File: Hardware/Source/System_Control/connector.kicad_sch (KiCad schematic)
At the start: 28 parts, among them J10 NTC_CONN, J11 NTC_CONN, J12 NTC_CONN, J13 NTC_CONN, J14 NTC_CONN, J15 NTC_CONN, J16 BAL_BAT_CONN2, J17 NTC_CONN, J18 NTC_CONN, J19 NTC_CONN, J20 NTC_CONN, J21 NTC_CONN, J22 NTC_CONN, J23 NTC_CONN, J24 NTC_CONN, J3 SIGNAL_CONN, J4 HB9500M-9.5-2P, J5 FLASH_CONN, J6 HB9500M-9.5-2P, J7 BAL_BAT_CONN1, J8 NTC_CONN, J9 NTC_CONN

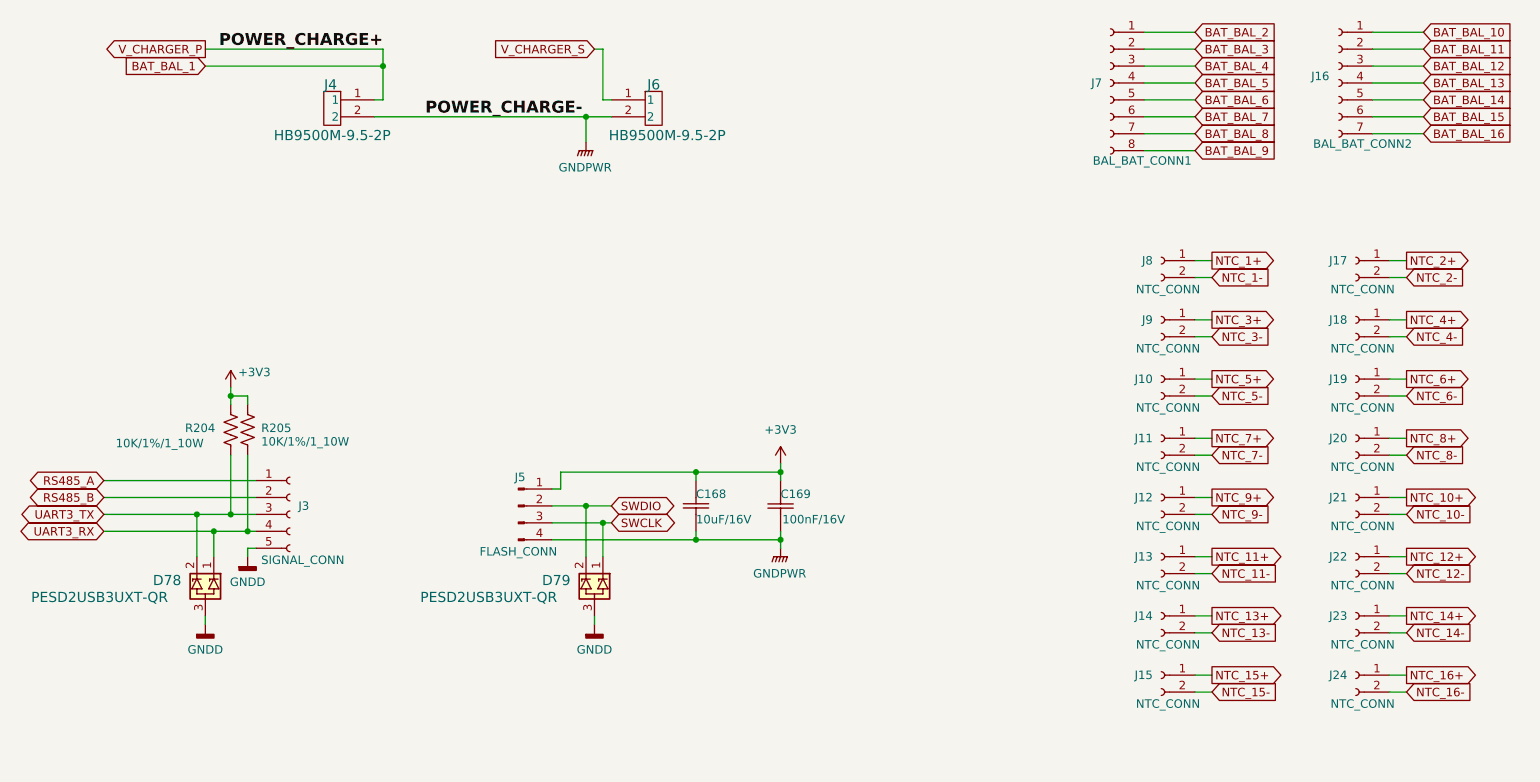
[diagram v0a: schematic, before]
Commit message: schematic: update connector charger board F4
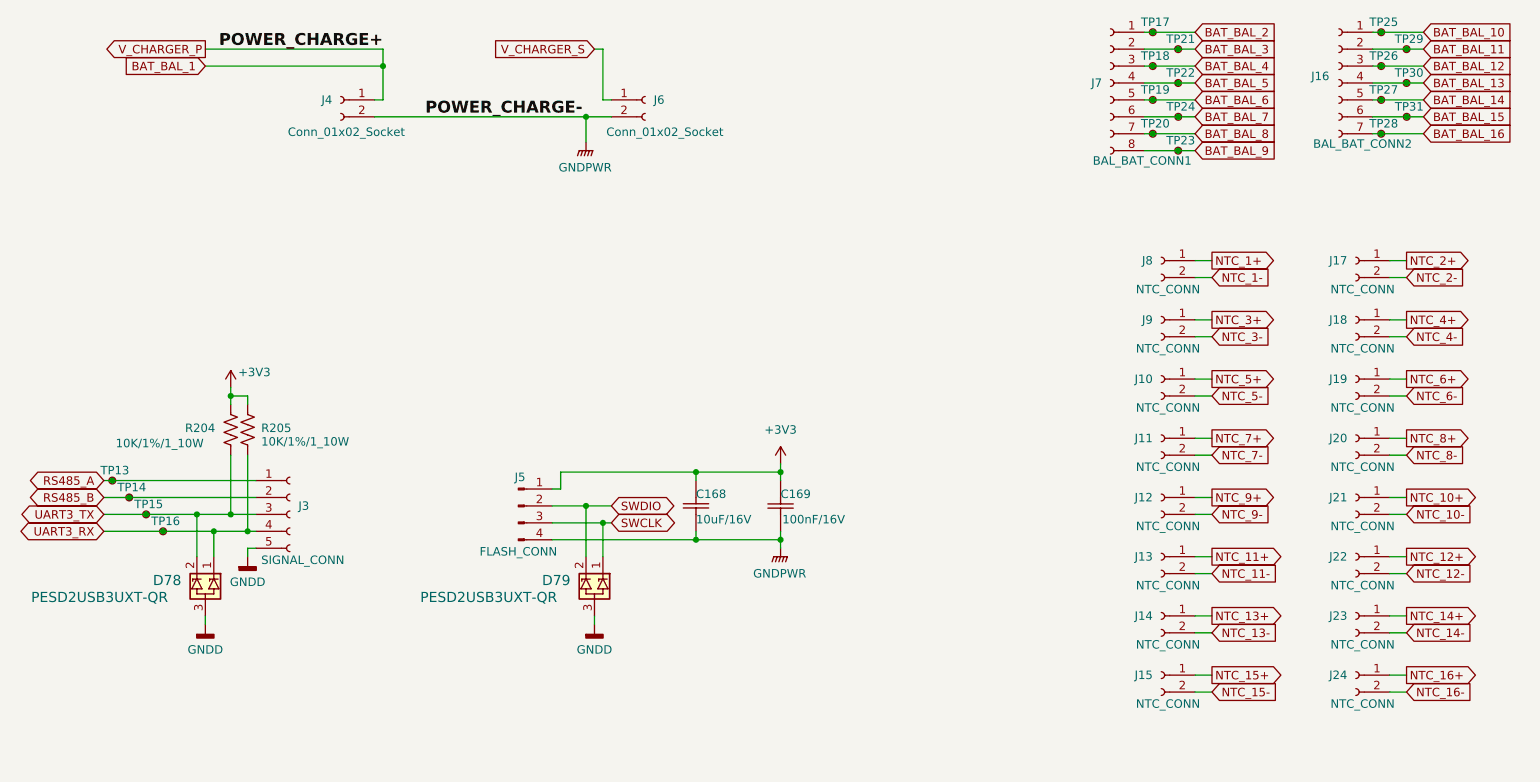
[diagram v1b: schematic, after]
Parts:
- removed J4, J6: HB9500M-9.5-2P, charge_battery_footprint_lib:CONN2_HB9500_KAN, symbol charge_battery_sym_lib:HB9500M-9.5-2P
- added J4, J6: Conn_01x02_Socket, Connector_Phoenix_MC:PhoenixContact_MC_1,5_2-G-3.81_1x02_P3.81mm_Horizontal, symbol Connector:Conn_01x02_Socket
- added TP13, TP14, TP15, TP16, TP17, TP18, TP19, TP20, TP21, TP22, TP23, TP24, TP25, TP26, TP27, TP28, TP29, TP30, TP31: TestPoint_Small, TestPoint:TestPoint_Pad_D1.0mm, symbol Connector:TestPoint_Small
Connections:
- net BAT_BAL_1: now also J4.1 (Pin_1)
- net BAT_BAL_10: now also TP25.1
- net BAT_BAL_11: now also TP29.1
- net BAT_BAL_12: now also TP26.1
- net BAT_BAL_13: now also TP30.1
- net BAT_BAL_14: now also TP27.1
- net BAT_BAL_15: now also TP31.1
- net BAT_BAL_16: now also TP28.1
- net BAT_BAL_2: now also TP17.1
- net BAT_BAL_3: now also TP21.1
- net BAT_BAL_4: now also TP18.1
- net BAT_BAL_5: now also TP22.1
- net BAT_BAL_6: now also TP19.1
- net BAT_BAL_7: now also TP24.1
- net BAT_BAL_8: now also TP20.1
- net BAT_BAL_9: now also TP23.1
- net GNDPWR: now also J4.2 (Pin_2), J6.2 (Pin_2)
- net RS485_A: now also TP13.1
- net RS485_B: now also TP14.1
- net UART3_RX: now also TP16.1
- net UART3_TX: now also TP15.1
- net V_CHARGER_S: now also J6.1 (Pin_1)

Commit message: pcb,lib,sche: PFC, lib: update pcb PFC, lib
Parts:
- renumbered C168 to C173, C169 to C174, D78 to D77, D79 to D78, R204 to R206, R205 to R207
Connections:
- net V_CHARGER_S is gone; now on net BAT_BAL_1: J6.1 (Pin_1)
- net BAT_BAL_1: no longer J4.1 (Pin_1)
- net BAT_BAL_10: now also J16.7 (Pin_7); no longer J16.1 (Pin_1)
- net BAT_BAL_11: now also J16.6 (Pin_6); no longer J16.2 (Pin_2)
- net BAT_BAL_12: now also J16.5 (Pin_5); no longer J16.3 (Pin_3)
- net BAT_BAL_14: now also J16.3 (Pin_3); no longer J16.5 (Pin_5)
- net BAT_BAL_15: now also J16.2 (Pin_2); no longer J16.6 (Pin_6)
- net BAT_BAL_16: now also J16.1 (Pin_1); no longer J16.7 (Pin_7)
- net BAT_BAL_2: now also J7.8 (Pin_8); no longer J7.1 (Pin_1)
- net BAT_BAL_3: now also J7.7 (Pin_7); no longer J7.2 (Pin_2)
- net BAT_BAL_4: now also J7.6 (Pin_6); no longer J7.3 (Pin_3)
- net BAT_BAL_5: now also J7.5 (Pin_5); no longer J7.4 (Pin_4)
- net BAT_BAL_6: now also J7.4 (Pin_4); no longer J7.5 (Pin_5)
- net BAT_BAL_7: now also J7.3 (Pin_3); no longer J7.6 (Pin_6)
- net BAT_BAL_8: now also J7.2 (Pin_2); no longer J7.7 (Pin_7)
- net BAT_BAL_9: now also J7.1 (Pin_1); no longer J7.8 (Pin_8)
- new net V_CHARGER_P: J4.1 (Pin_1)

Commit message: 3d:lib:update 3d model heatsink
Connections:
- net GNDPWR: now also J4.1 (Pin_1); no longer J4.2 (Pin_2)
- net V_CHARGER_P: now also J4.2 (Pin_2); no longer J4.1 (Pin_1)
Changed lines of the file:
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@@
 	(symbol
 		(lib_id "Connector:Conn_01x02_Socket")
-		(at 83.82 50.8 0)
-		(mirror y)
-		(unit 1)
-		(exclude_from_sim no)
-		(in_bom yes)
-		(on_board yes)
-		(dnp no)
-		(property "Reference" "J4"
-			(at 82.55 50.7999 0)
-			(effects
-				(font
-					(size 1.27 1.27)
-				)
-				(justify left)
-			)
-		)
-		(property "Value" "Conn_01x02_Socket"
-			(at 93.472 55.626 0)
-			(effects
-				(font
-					(size 1.27 1.27)
-				)
-				(justify left)
-			)
-		)
-		(property "Footprint" "Connector_Phoenix_MC:PhoenixContact_MC_1,5_2-G-3.81_1x02_P3.81mm_Horizontal"
-			(at 83.82 50.8 0)
-			(effects
-				(font
-					(size 1.27 1.27)
-				)
-				(hide yes)
-			)
-		)
-		(property "Datasheet" "~"
-			(at 83.82 50.8 0)
-			(effects
-				(font
-					(size 1.27 1.27)
-				)
-				(hide yes)
-			)
-		)
-		(property "Description" "Generic connector, single row, 01x02, script generated"
-			(at 83.82 50.8 0)
-			(effects
-				(font
-					(size 1.27 1.27)
-				)
-				(hide yes)
-			)
-		)
-		(property "Supply URL" "https://www.thegioiic.com/ul-3-81-2-r-terminal-block-plug-in-han-pcb-2-chan-cong-3-81mm-300v-10a-ulo"
-			(at 83.82 50.8 0)
-			(effects
-				(font
-					(size 1.27 1.27)
-				)
-				(hide yes)
-			)
-		)
-		(property "Supply name" "Thegioiic"
-			(at 83.82 50.8 0)
-			(effects
-				(font
-					(size 1.27 1.27)
-				)
-				(hide yes)
-			)
-		)
-		(pin "1"
-		)
-		(pin "2"
-		)
-		(instances
-			(project "System_Control"
-				(path "/85c53e8c-0403-413d-b6c5-0718d4365b1f/3a5f6f4d-7ae8-4d5e-869b-e74be22e0b12"
-					(reference "J4")
-					(unit 1)
-				)
-			)
-		)
-	)
-	(symbol
-		(lib_id "Connector:Conn_01x02_Socket")
 		(at 236.22 101.6 0)
 		(mirror y)
@@
 					(unit 1)
 				)
+			)
+		)
+	)
+	(symbol
+		(lib_id "Connector:Conn_01x02_Socket")
+		(at 83.82 53.34 180)
+		(unit 1)
+		(exclude_from_sim no)
+		(in_bom yes)
+		(on_board yes)
+		(dnp no)
+		(property "Reference" "J4"
+			(at 82.55 53.3401 0)
+			(effects
+				(font
+					(size 1.27 1.27)
+				)
+				(justify left)
+			)
+		)
+		(property "Value" "Conn_01x02_Socket"
+			(at 94.996 55.118 0)
+			(effects
+				(font
+					(size 1.27 1.27)
+				)
+				(justify left)
+			)
+		)
+		(property "Footprint" "Connector_Phoenix_MC:PhoenixContact_MC_1,5_2-G-3.81_1x02_P3.81mm_Horizontal"
+			(at 83.82 53.34 0)
+			(effects
+				(font
+					(size 1.27 1.27)
+				)
+				(hide yes)
+			)
+		)
+		(property "Datasheet" "~"
+			(at 83.82 53.34 0)
+			(effects
+				(font
+					(size 1.27 1.27)
+				)
+				(hide yes)
+			)
+		)
+		(property "Description" "Generic connector, single row, 01x02, script generated"
+			(at 83.82 53.34 0)
+			(effects
+				(font
+					(size 1.27 1.27)
+				)
+				(hide yes)
+			)
+		)
+		(property "Supply URL" "https://www.thegioiic.com/ul-3-81-2-r-terminal-block-plug-in-han-pcb-2-chan-cong-3-81mm-300v-10a-ulo"
+			(at 83.82 53.34 0)
+			(effects
+				(font
+					(size 1.27 1.27)
+				)
+				(hide yes)
+			)
+		)
+		(property "Supply name" "Thegioiic"
+			(at 83.82 53.34 0)
+			(effects
+				(font
+					(size 1.27 1.27)
+				)
+				(hide yes)
+			)
+		)
+		(pin "1"
+		)
+		(pin "2"
+		)
+		(instances
+			(project "System_Control"
+				(path "/85c53e8c-0403-413d-b6c5-0718d4365b1f/3a5f6f4d-7ae8-4d5e-869b-e74be22e0b12"
+					(reference "J4")
+					(unit 1)
+				)

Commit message: pull
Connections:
- net RS485_A renamed RS485_P
- net RS485_B renamed RS485_N
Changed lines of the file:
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@@
 		)
 	)
-	(global_label "RS485_B"
+	(global_label "RS485_N"
 		(shape bidirectional)
 		(at 48.26 110.49 180)
@@
 		)
 		(property "Intersheetrefs" "${INTERSHEET_REFS}"
-			(at 35.8179 110.49 0)
+			(at 35.7574 110.49 0)
 			(effects
 				(font
@@
 		)
 	)
-	(global_label "RS485_A"
+	(global_label "RS485_P"
 		(shape bidirectional)
 		(at 48.26 107.95 180)
@@
 		)
 		(property "Intersheetrefs" "${INTERSHEET_REFS}"
-			(at 35.9993 107.95 0)
-			(effects
-				(font
+			(at 35.8179 107.95 0)
+			(effects
+				(font

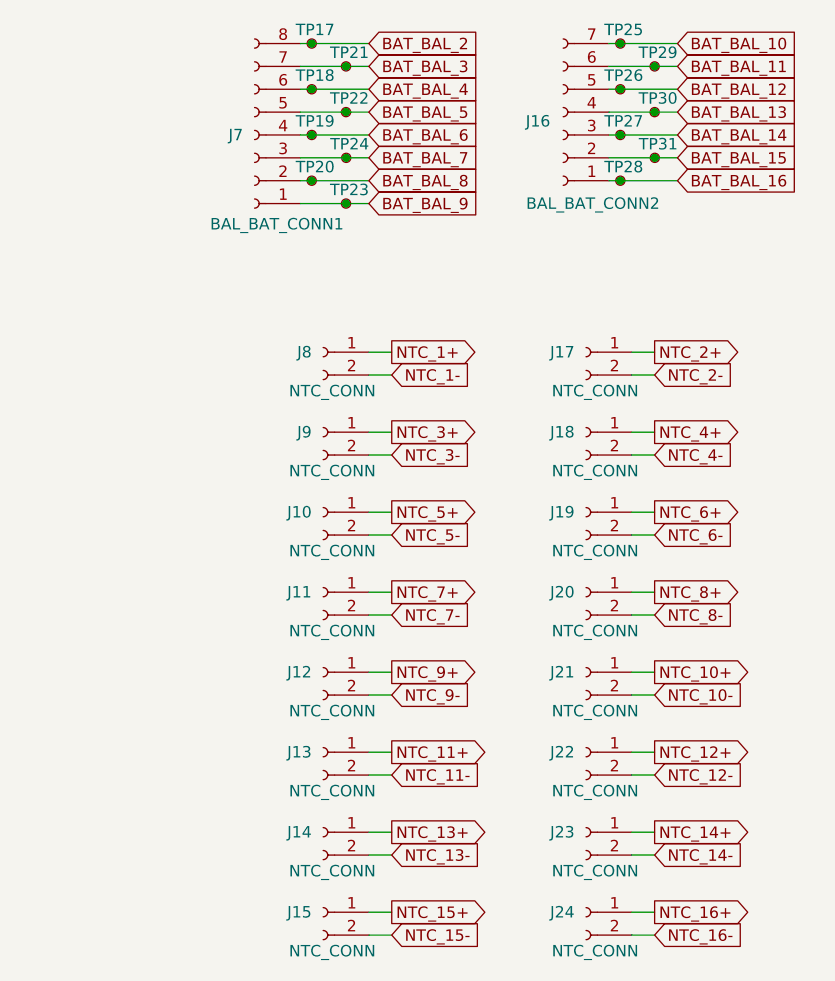
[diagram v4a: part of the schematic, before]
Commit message: footprint:lib:update header xh2.54 8pin smd
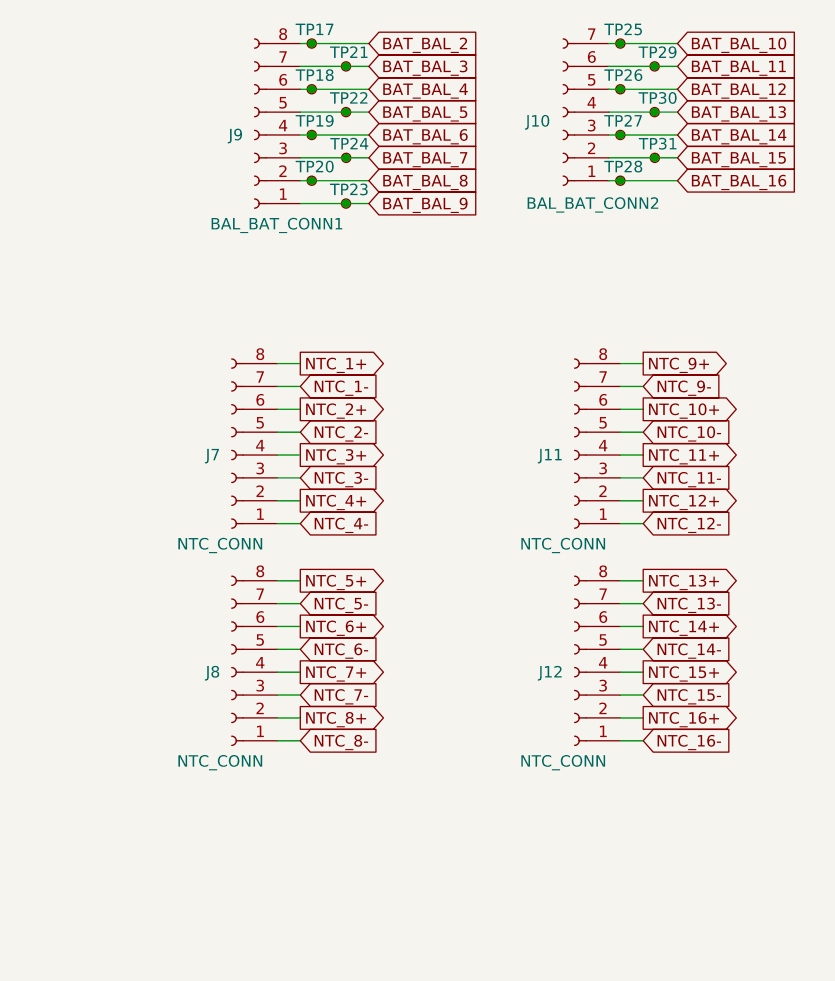
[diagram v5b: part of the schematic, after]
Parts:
- removed J10, J11, J12, J13, J14, J15, J17, J18, J19, J20, J21, J22, J23, J24, J8, J9: NTC_CONN, charge_battery_footprint_lib:XH_2.54mm_2_SMD, symbol Connector:Conn_01x02_Socket
- added J11, J12, J7, J8: NTC_CONN, charge_battery_footprint_lib:XH_2.54mm_8_SMD, symbol Connector:Conn_01x08_Socket
- renumbered J16 to J10, J7 to J9
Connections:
- net NTC_1+: now also J7.8 (Pin_8)
- net NTC_1-: now also J7.7 (Pin_7)
- net NTC_10+: now also J11.6 (Pin_6)
- net NTC_10-: now also J11.5 (Pin_5)
- net NTC_11+: now also J11.4 (Pin_4)
- net NTC_11-: now also J11.3 (Pin_3)
- net NTC_12+: now also J11.2 (Pin_2)
- net NTC_12-: now also J11.1 (Pin_1)
- net NTC_13+: now also J12.8 (Pin_8)
- net NTC_13-: now also J12.7 (Pin_7)
- net NTC_14+: now also J12.6 (Pin_6)
- net NTC_14-: now also J12.5 (Pin_5)
- net NTC_15+: now also J12.4 (Pin_4)
- net NTC_15-: now also J12.3 (Pin_3)
- net NTC_16+: now also J12.2 (Pin_2)
- net NTC_16-: now also J12.1 (Pin_1)
- net NTC_2+: now also J7.6 (Pin_6)
- net NTC_2-: now also J7.5 (Pin_5)
- net NTC_3+: now also J7.4 (Pin_4)
- net NTC_3-: now also J7.3 (Pin_3)
- net NTC_4+: now also J7.2 (Pin_2)
- net NTC_4-: now also J7.1 (Pin_1)
- net NTC_5+: now also J8.8 (Pin_8)
- net NTC_5-: now also J8.7 (Pin_7)
- net NTC_6+: now also J8.6 (Pin_6)
- net NTC_6-: now also J8.5 (Pin_5)
- net NTC_7+: now also J8.4 (Pin_4)
- net NTC_7-: now also J8.3 (Pin_3)
- net NTC_8+: now also J8.2 (Pin_2)
- net NTC_8-: now also J8.1 (Pin_1)
- net NTC_9+: now also J11.8 (Pin_8)
- net NTC_9-: now also J11.7 (Pin_7)
